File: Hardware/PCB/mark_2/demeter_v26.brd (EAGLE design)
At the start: 90 x 56 mm, 70 parts, among them IC1 4050, IC2 LM1117-5.0, IC3 LM1117-3.3, IC5 MCP3424, IC6 MCP23017SO, IC8 ATMEGA32U4-AU, Q1 IRLML6402, Q3 IRLML6402, Q5 IRLML6402

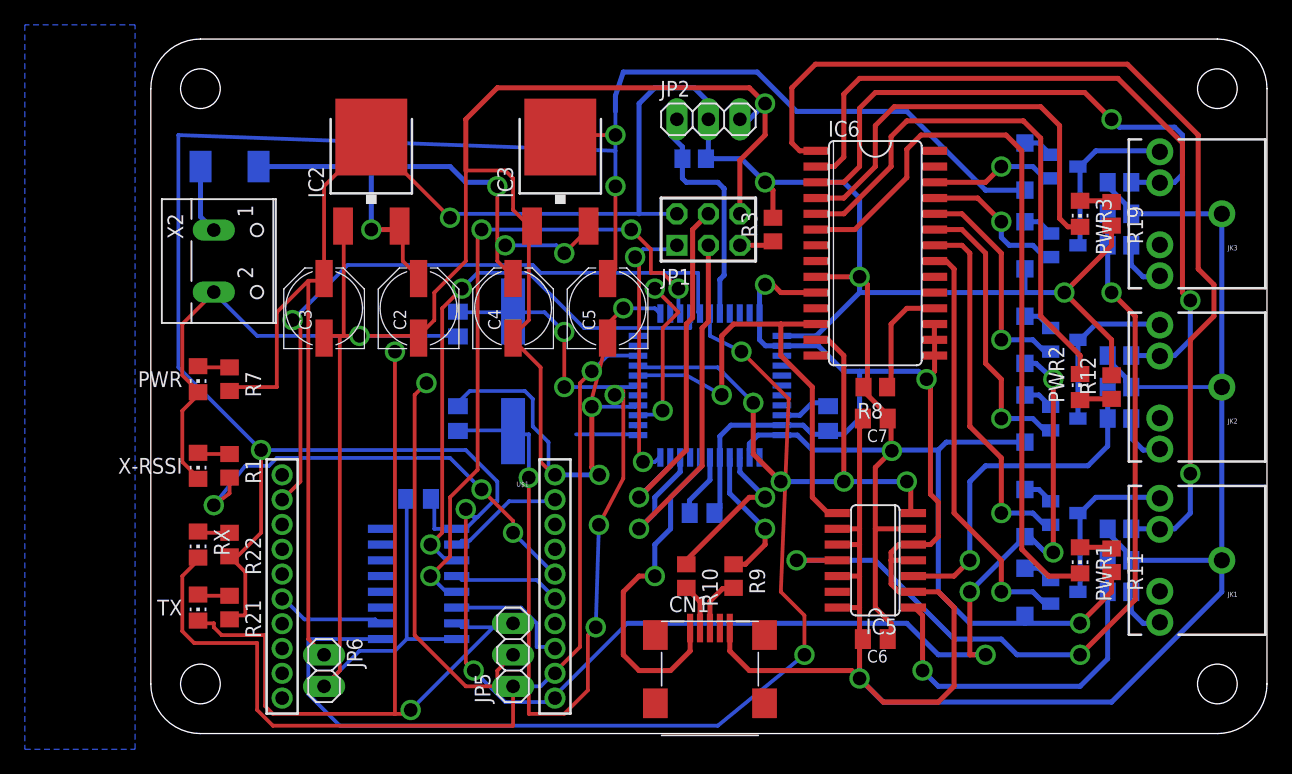
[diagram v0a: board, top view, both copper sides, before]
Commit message: 
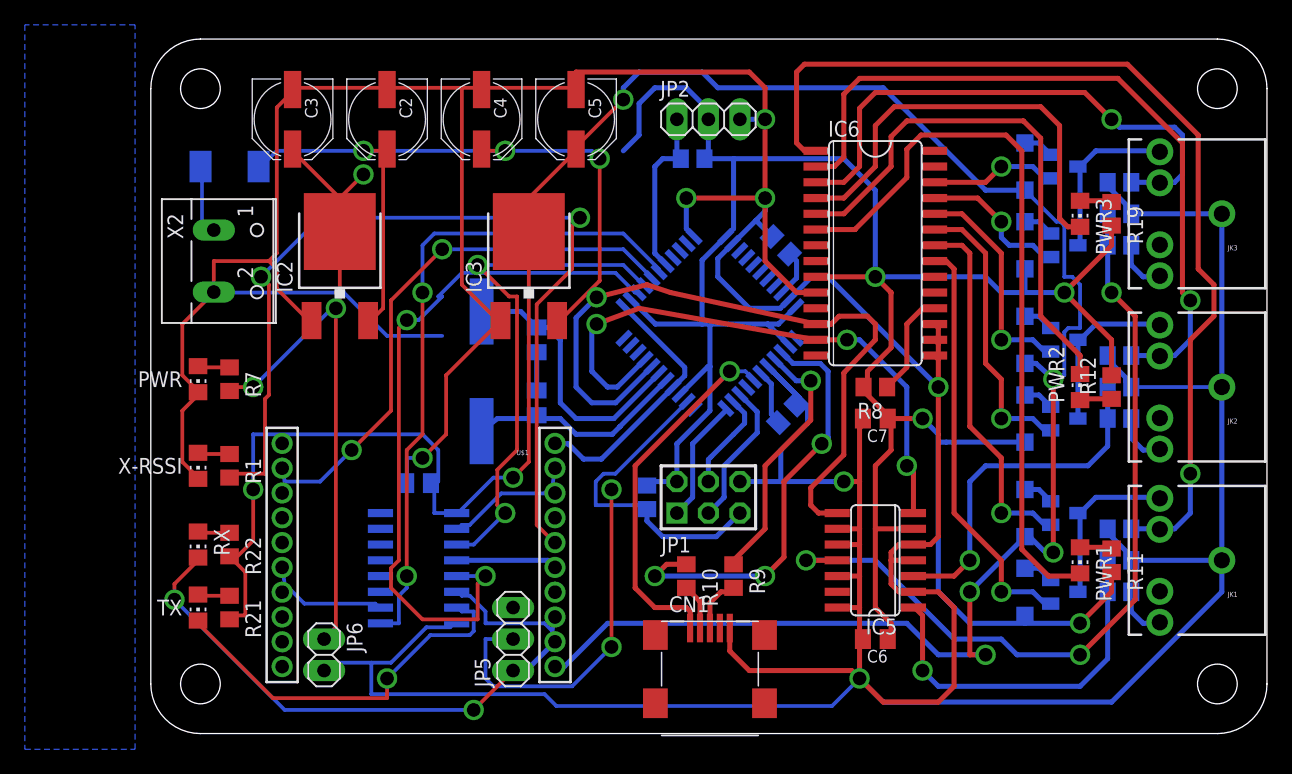
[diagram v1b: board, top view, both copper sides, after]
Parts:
- moved R3 23.9 mm to (41.3, 20.3), flipped to the bottom
- moved JP1 21.6 mm to (46.2, 20.3)
- moved C3 15.5 mm to (12.7, 50.8), turned to 270 degrees
- moved C2 15.5 mm to (20.3, 50.8), turned to 270 degrees
- moved C4 15.5 mm to (27.9, 50.8), turned to 270 degrees
- moved C5 15.5 mm to (35.6, 50.8), turned to 270 degrees
- moved C8 14.5 mm to (52.1, 40.6), turned to 45 degrees
- moved C1 10.5 mm to (52.6, 27.1), turned to 135 degrees
- moved IC2 8.03 mm to (16.5, 39.4)
- moved IC3 8.03 mm to (31.8, 39.4)
- moved C10 6.48 mm to (32.4, 27.9)
- moved C9 6.48 mm to (32.4, 33.0)
- moved IC8 5.08 mm to (46.4, 34.4), turned to 45 degrees
- moved U$1 2.54 mm to (22.9, 26.7)
- moved Q9 2.54 mm to (27.9, 30.5)
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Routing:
- net +3V3: track 261.6 -> 207.9 mm, vias 9 -> 7
- net N$27: track 59.9 -> 18.0 mm, vias 4 -> 0
- net RSSI: track 36.6 -> 75.4 mm, vias 3 -> 2
- net TX: track 68.0 -> 31.2 mm, vias 2 -> 1
- net RX: track 76.2 -> 40.8 mm, vias 1 -> 2
- net RTS: track 84.8 -> 53.6 mm
- net GND: track 471.4 -> 500.7 mm, vias 8 -> 7
- net RST: track 3.05 -> 26.2 mm
- net D-: track 13.4 -> 35.1 mm, vias 1 -> 3
- net MOSI: track 29.5 -> 8.07 mm, vias 1 -> 0
- net SCL: track 37.5 -> 58.4 mm
- net SCK: track 32.3 -> 11.8 mm, vias 1 -> 0
- net +5V: track 281.3 -> 261.0 mm, vias 8 -> 7
- net +12V: track 49.1 -> 61.6 mm, vias 4 -> 3
- net MISO: track 22.1 -> 10.1 mm, vias 2 -> 0
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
